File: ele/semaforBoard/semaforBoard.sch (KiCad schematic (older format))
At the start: 25 parts, among them J1 RESET, J2 Flash_connector, J3 USB_A, Q1 BC817, Q2 BC817, Q3 BC817, SW1 SW_Push, U1 ESP-01, U2 AMS1117-3.3

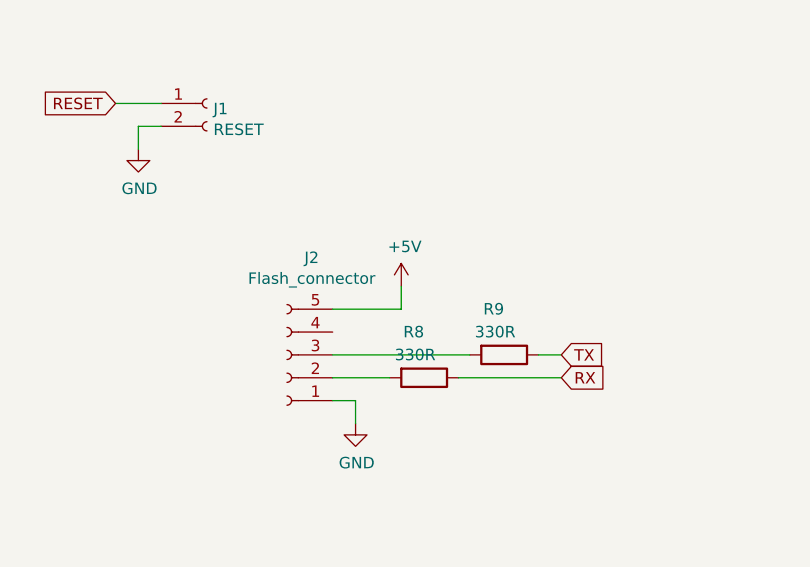
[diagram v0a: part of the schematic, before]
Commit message: Component placement, logos.
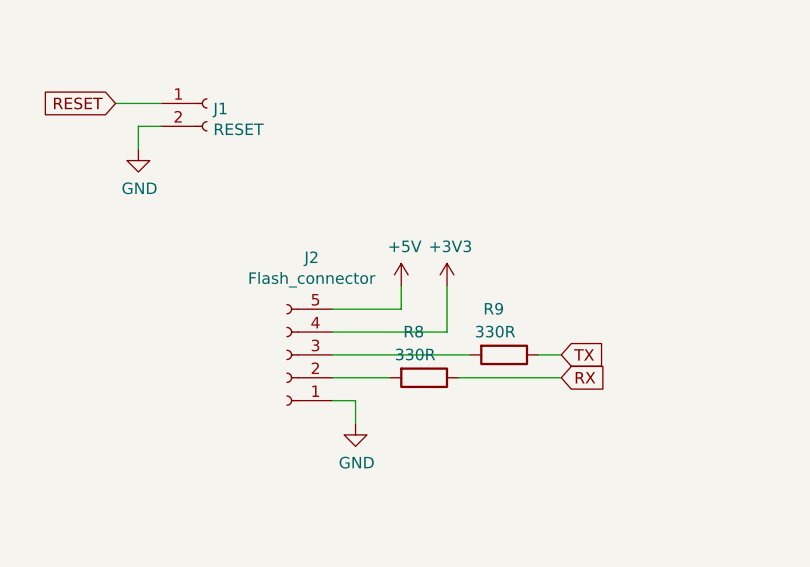
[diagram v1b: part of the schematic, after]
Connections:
- net +3V3: now also J2.4 (Pin_4)
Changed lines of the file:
@@
 	1    0    0    -1
 $EndComp
+$Comp
+L power:+3V3 #PWR?
+U 1 1 5ED38F5D
+P 6550 4250
+F 0 "#PWR?" H 6550 4100 50  0001 C CNN
+F 1 "+3V3" H 6565 4423 50  0000 C CNN
+F 2 "" H 6550 4250 50  0001 C CNN
+F 3 "" H 6550 4250 50  0001 C CNN
+	1    6550 4250
+	1    0    0    -1
+$EndComp
+Wire Wire Line
+	6550 4250 6550 4450
+Wire Wire Line
+	6550 4450 6050 4450
 $EndSCHEMATC

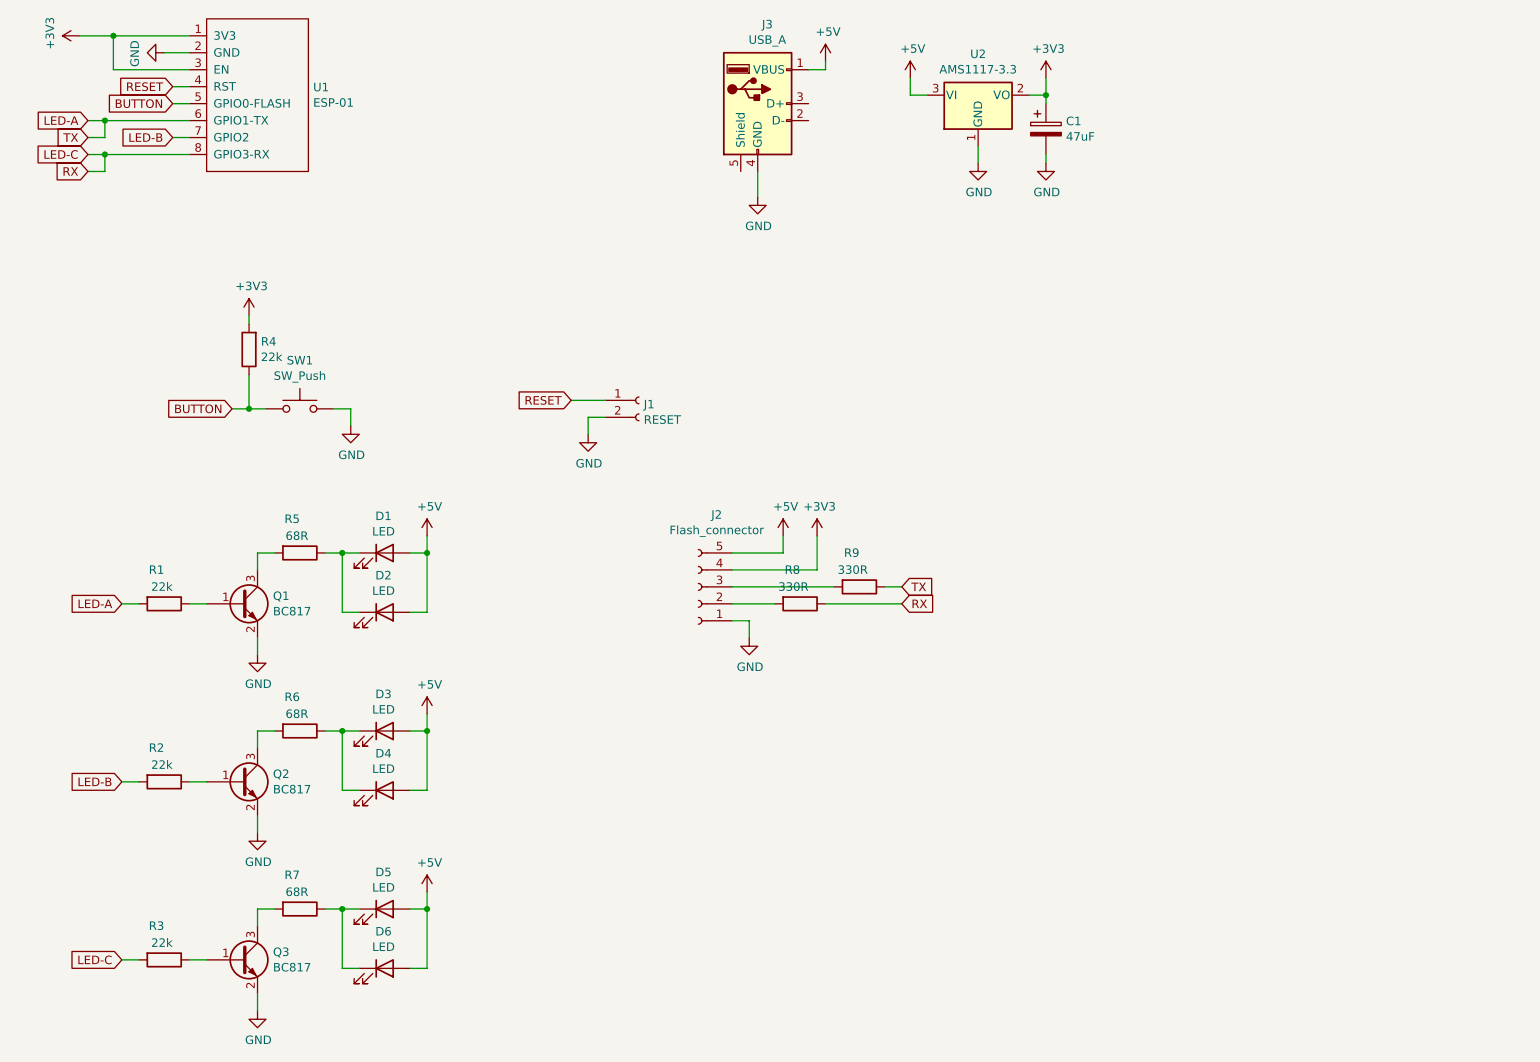
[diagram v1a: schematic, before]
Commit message: Updated schmatic for CH340G.
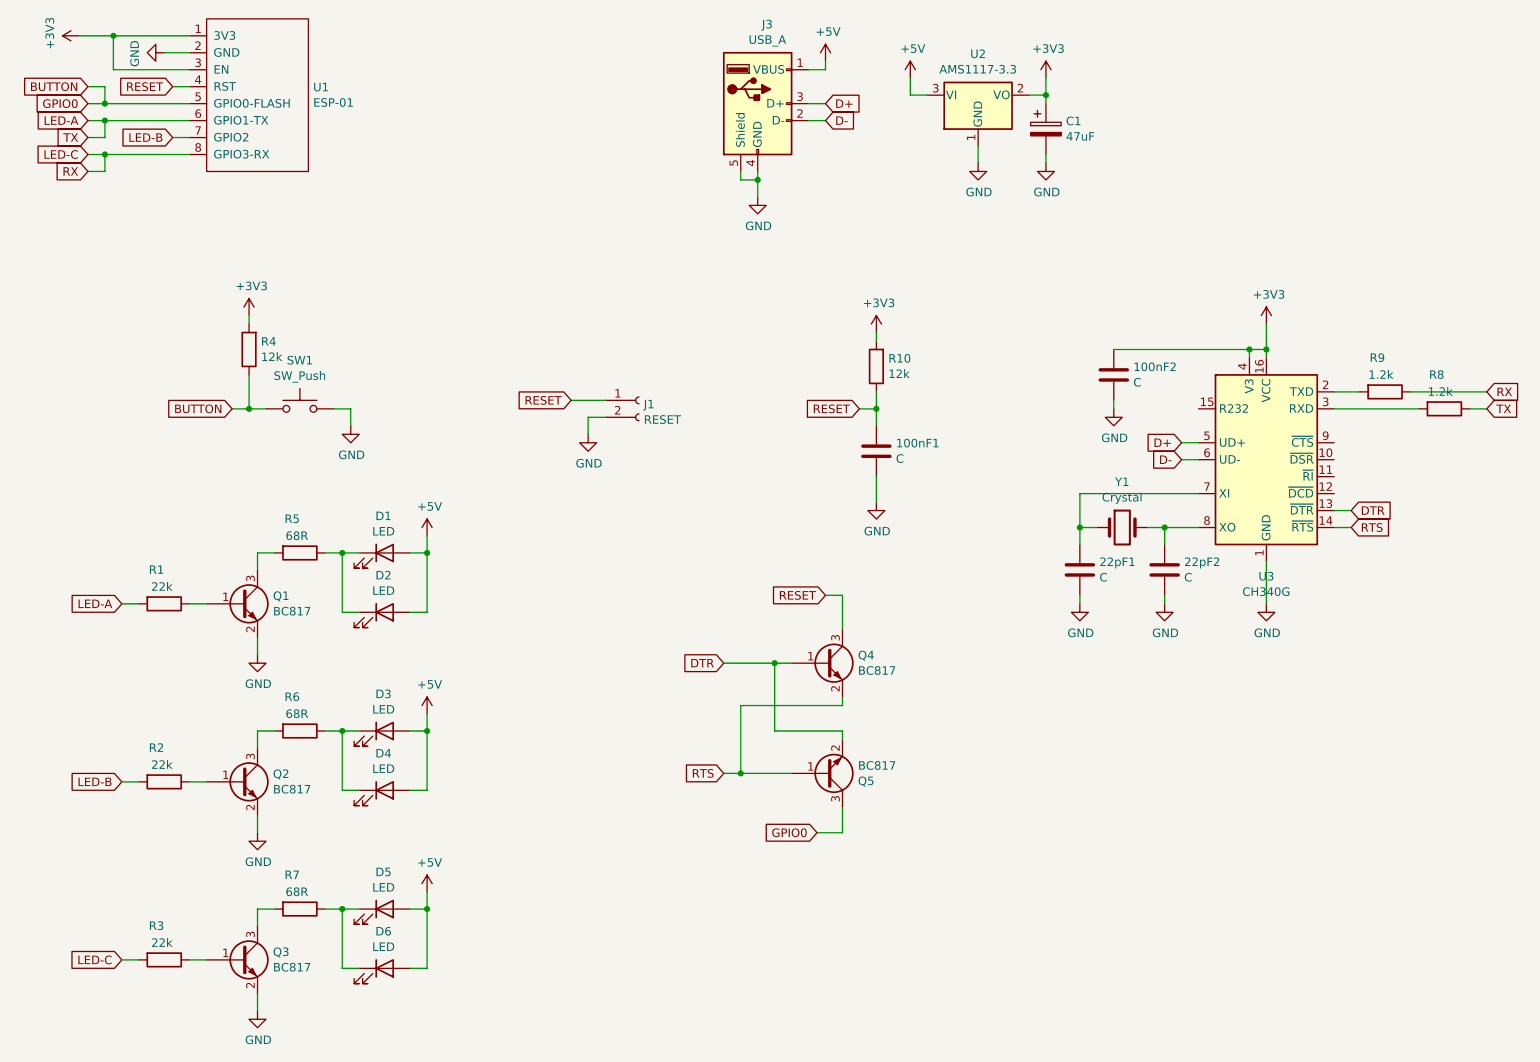
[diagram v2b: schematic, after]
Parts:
- removed J2: Flash_connector, semaforBoard:PinHeader_1x05_P2.54mm_Vertical, symbol Connector:Conn_01x05_Female
- added 100nF1, 100nF2, 22pF1, 22pF2: C, Capacitor_SMD:C_1206_3216Metric_Pad1.42x1.75mm_HandSolder, symbol Device:C
- added Q4, Q5: BC817, Package_TO_SOT_SMD:SOT-23, symbol Transistor_BJT:BC817
- added R10: 12k, Resistor_SMD:R_1206_3216Metric_Pad1.42x1.75mm_HandSolder, symbol Device:R
- added U3: CH340G, Package_SO:SOIC-16_3.9x9.9mm_P1.27mm, symbol Interface_USB:CH340G
- added Y1: Crystal, Crystal:Crystal_HC49-4H_Vertical, symbol Device:Crystal
- J1: footprint Resistor_SMD:R_1206_3216Metric_Pad1.42x1.75mm_HandSolder -> Connector_PinHeader_2.54mm:PinHeader_1x02_P2.54mm_Vertical
- R4: value 22k -> 12k
- R8, R9: value 330R -> 1.2k
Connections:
- net +3V3: now also 100nF2.1, R10.2, U3.16 (VCC), U3.4 (V3)
- net BUTTON: now also Q5.3 (C)
- net GND: now also J3.5 (Shield), 100nF1.2, 100nF2.2, 22pF1.2, 22pF2.2, U3.1 (GND)
- net LED-A: now also R8.1; no longer R9.1
- net LED-C: now also R9.1; no longer R8.1
- net RESET: now also 100nF1.1, Q4.3 (C), R10.1
- net D-: now reaches J3.2 (D-)
- net D-: now also U3.6 (UD-)
- net D+: now reaches J3.3 (D+)
- net D+: now also U3.5 (UD+)
- net at R8.2: now also U3.3 (RXD)
- net at R9.2: now also U3.2 (TXD)
- new net: 22pF1.1, U3.7 (XI), Y1.1
- new net: 22pF2.1, U3.8 (XO), Y1.2
- new net DTR: Q4.1 (B), Q5.2 (E), U3.13 (~DTR)
- new net RTS: Q4.2 (E), Q5.1 (B), U3.14 (~RTS)
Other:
- moved on the sheet: R8, R9

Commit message: 10mm leds. PCB routed.
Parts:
- C: renamed from 22pF1; value C -> 22pF
- C: renamed from 22pF2; value C -> 22pF
- C: renamed from 100nF2; value C -> 100nF
- C: renamed from 100nF1; value C -> 100nF
- D1, D2, D3, D4, D5, D6: footprint LED_THT:LED_D8.0mm -> LED_THT:LED_D10.0mm
- J1: footprint Connector_PinHeader_2.54mm:PinHeader_1x02_P2.54mm_Vertical -> semaforBoard:PinHeader_1x02_P2.54mm_Vertical
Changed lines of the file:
@@
 F 0 "D1" H 3993 4567 50  0000 C CNN
 F 1 "LED" H 3993 4476 50  0000 C CNN
-F 2 "LED_THT:LED_D8.0mm" H 4000 4350 50  0001 C CNN
+F 2 "LED_THT:LED_D10.0mm" H 4000 4350 50  0001 C CNN
 F 3 "~" H 4000 4350 50  0001 C CNN
 	1    4000 4350
@@
 F 0 "D2" H 3993 4917 50  0000 C CNN
 F 1 "LED" H 3993 4826 50  0000 C CNN
-F 2 "LED_THT:LED_D8.0mm" H 4000 4700 50  0001 C CNN
+F 2 "LED_THT:LED_D10.0mm" H 4000 4700 50  0001 C CNN
 F 3 "~" H 4000 4700 50  0001 C CNN
 	1    4000 4700
@@
 F 0 "D3" H 3993 5617 50  0000 C CNN
 F 1 "LED" H 3993 5526 50  0000 C CNN
-F 2 "LED_THT:LED_D8.0mm" H 4000 5400 50  0001 C CNN
+F 2 "LED_THT:LED_D10.0mm" H 4000 5400 50  0001 C CNN
 F 3 "~" H 4000 5400 50  0001 C CNN
 	1    4000 5400
@@
 F 0 "D4" H 3993 5967 50  0000 C CNN
 F 1 "LED" H 3993 5876 50  0000 C CNN
-F 2 "LED_THT:LED_D8.0mm" H 4000 5750 50  0001 C CNN
+F 2 "LED_THT:LED_D10.0mm" H 4000 5750 50  0001 C CNN
 F 3 "~" H 4000 5750 50  0001 C CNN
 	1    4000 5750
@@
 F 0 "D5" H 3993 6667 50  0000 C CNN
 F 1 "LED" H 3993 6576 50  0000 C CNN
-F 2 "LED_THT:LED_D8.0mm" H 4000 6450 50  0001 C CNN
+F 2 "LED_THT:LED_D10.0mm" H 4000 6450 50  0001 C CNN
 F 3 "~" H 4000 6450 50  0001 C CNN
 	1    4000 6450
@@
 F 0 "D6" H 3993 7017 50  0000 C CNN
 F 1 "LED" H 3993 6926 50  0000 C CNN
-F 2 "LED_THT:LED_D8.0mm" H 4000 6800 50  0001 C CNN
+F 2 "LED_THT:LED_D10.0mm" H 4000 6800 50  0001 C CNN
 F 3 "~" H 4000 6800 50  0001 C CNN
 	1    4000 6800
@@
 	5200 3550 5300 3550
 $Comp
-L Connector:Conn_01x02_Female J1
-U 1 1 5ECA02FE
-P 5500 3450
-F 0 "J1" H 5528 3426 50  0000 L CNN
-F 1 "RESET" H 5528 3335 50  0000 L CNN
-F 2 "Connector_PinHeader_2.54mm:PinHeader_1x02_P2.54mm_Vertical" H 5500 3450 50  0001 C CNN
-F 3 "~" H 5500 3450 50  0001 C CNN
-	1    5500 3450
-	1    0    0    -1
-$EndComp
-$Comp
 L Device:R R8
 U 1 1 5ECACA5D
@@
 $EndComp
 $Comp
-L Device:C 22pF1
+L Device:C C
 U 1 1 5EE8F2DB
 P 8100 4450
-F 0 "22pF1" H 8215 4496 50  0000 L CNN
-F 1 "C" H 8215 4405 50  0000 L CNN
+F 0 "C" H 8215 4496 50  0000 L CNN
+F 1 "22pF" H 8215 4405 50  0000 L CNN
 F 2 "Capacitor_SMD:C_1206_3216Metric_Pad1.42x1.75mm_HandSolder" H 8138 4300 50  0001 C CNN
 F 3 "~" H 8100 4450 50  0001 C CNN
@@
 $EndComp
 $Comp
-L Device:C 22pF2
+L Device:C C
 U 1 1 5EE90BE3
 P 8600 4450
-F 0 "22pF2" H 8715 4496 50  0000 L CNN
-F 1 "C" H 8715 4405 50  0000 L CNN
+F 0 "C" H 8715 4496 50  0000 L CNN
+F 1 "22pF" H 8715 4405 50  0000 L CNN
 F 2 "Capacitor_SMD:C_1206_3216Metric_Pad1.42x1.75mm_HandSolder" H 8638 4300 50  0001 C CNN
 F 3 "~" H 8600 4450 50  0001 C CNN
@@
 	9200 3150 9200 3200
 $Comp
-L Device:C 100nF2
+L Device:C C
 U 1 1 5EEBA62B
 P 8300 3300
-F 0 "100nF2" H 8415 3346 50  0000 L CNN
-F 1 "C" H 8415 3255 50  0000 L CNN
+F 0 "C" H 8415 3346 50  0000 L CNN
+F 1 "100nF" H 8415 3255 50  0000 L CNN
 F 2 "Capacitor_SMD:C_1206_3216Metric_Pad1.42x1.75mm_HandSolder" H 8338 3150 50  0001 C CNN
 F 3 "~" H 8300 3300 50  0001 C CNN
@@
 RESET
 $Comp
-L Device:C 100nF1
-U 1 1 5EEE7618
-P 6900 3750
-F 0 "100nF1" H 7015 3796 50  0000 L CNN
-F 1 "C" H 7015 3705 50  0000 L CNN
-F 2 "Capacitor_SMD:C_1206_3216Metric_Pad1.42x1.75mm_HandSolder" H 6938 3600 50  0001 C CNN
-F 3 "~" H 6900 3750 50  0001 C CNN
-	1    6900 3750
-	1    0    0    -1
-$EndComp
-$Comp
 L power:GND #PWR0124
 U 1 1 5EEEFA1C
@@
 Wire Wire Line
 	6900 3500 6900 3600
+$Comp
+L Device:C C
+U 1 1 5EEE7618
+P 6900 3750
+F 0 "C" H 7015 3796 50  0000 L CNN
+F 1 "100nF" H 7015 3705 50  0000 L CNN
+F 2 "Capacitor_SMD:C_1206_3216Metric_Pad1.42x1.75mm_HandSolder" H 6938 3600 50  0001 C CNN
+F 3 "~" H 6900 3750 50  0001 C CNN
+	1    6900 3750
+	1    0    0    -1
+$EndComp
+$Comp
+L Connector:Conn_01x02_Female J1
+U 1 1 5ECA02FE
+P 5500 3450
+F 0 "J1" H 5528 3426 50  0000 L CNN
+F 1 "RESET" H 5528 3335 50  0000 L CNN
+F 2 "semaforBoard:PinHeader_1x02_P2.54mm_Vertical" H 5500 3450 50  0001 C CNN
+F 3 "~" H 5500 3450 50  0001 C CNN
+	1    5500 3450
+	1    0    0    -1
+$EndComp
 $EndSCHEMATC

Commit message: Panelized using kikit and generated fabrication data.
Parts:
- R1, R2, R3: value 22k -> 10k
- R10, R4: value 12k -> 10k
- R5, R6, R7: value 68R -> 75R
- R8, R9: value 1.2k -> 1k
- renumbered C to C2, C to C3, C to C4, C to C5
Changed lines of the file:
@@
 P 3200 3150
 F 0 "R4" H 3130 3104 50  0000 R CNN
-F 1 "12k" H 3130 3195 50  0000 R CNN
+F 1 "10k" H 3130 3195 50  0000 R CNN
 F 2 "Resistor_SMD:R_1206_3216Metric_Pad1.42x1.75mm_HandSolder" V 3130 3150 50  0001 C CNN
 F 3 "~" H 3200 3150 50  0001 C CNN
@@
 P 3500 4350
 F 0 "R5" V 3300 4350 50  0000 R CNN
-F 1 "68R" V 3400 4400 50  0000 R CNN
+F 1 "75R" V 3400 4400 50  0000 R CNN
 F 2 "Resistor_SMD:R_1206_3216Metric_Pad1.42x1.75mm_HandSolder" V 3430 4350 50  0001 C CNN
 F 3 "~" H 3500 4350 50  0001 C CNN
@@
 P 2700 4650
 F 0 "R1" V 2500 4650 50  0000 R CNN
-F 1 "22k" V 2600 4700 50  0000 R CNN
+F 1 "10k" V 2600 4700 50  0000 R CNN
 F 2 "Resistor_SMD:R_1206_3216Metric_Pad1.42x1.75mm_HandSolder" V 2630 4650 50  0001 C CNN
 F 3 "~" H 2700 4650 50  0001 C CNN
@@
 P 3500 5400
 F 0 "R6" V 3300 5400 50  0000 R CNN
-F 1 "68R" V 3400 5450 50  0000 R CNN
+F 1 "75R" V 3400 5450 50  0000 R CNN
 F 2 "Resistor_SMD:R_1206_3216Metric_Pad1.42x1.75mm_HandSolder" V 3430 5400 50  0001 C CNN
 F 3 "~" H 3500 5400 50  0001 C CNN
@@
 P 2700 5700
 F 0 "R2" V 2500 5700 50  0000 R CNN
-F 1 "22k" V 2600 5750 50  0000 R CNN
+F 1 "10k" V 2600 5750 50  0000 R CNN
 F 2 "Resistor_SMD:R_1206_3216Metric_Pad1.42x1.75mm_HandSolder" V 2630 5700 50  0001 C CNN
 F 3 "~" H 2700 5700 50  0001 C CNN
@@
 P 3500 6450
 F 0 "R7" V 3300 6450 50  0000 R CNN
-F 1 "68R" V 3400 6500 50  0000 R CNN
+F 1 "75R" V 3400 6500 50  0000 R CNN
 F 2 "Resistor_SMD:R_1206_3216Metric_Pad1.42x1.75mm_HandSolder" V 3430 6450 50  0001 C CNN
 F 3 "~" H 3500 6450 50  0001 C CNN
@@
 P 2700 6750
 F 0 "R3" V 2500 6750 50  0000 R CNN
-F 1 "22k" V 2600 6800 50  0000 R CNN
+F 1 "10k" V 2600 6800 50  0000 R CNN
 F 2 "Resistor_SMD:R_1206_3216Metric_Pad1.42x1.75mm_HandSolder" V 2630 6750 50  0001 C CNN
 F 3 "~" H 2700 6750 50  0001 C CNN
@@
 P 10250 3500
 F 0 "R8" V 10050 3500 50  0000 R CNN
-F 1 "1.2k" V 10150 3550 50  0000 R CNN
+F 1 "1k" V 10150 3550 50  0000 R CNN
 F 2 "Resistor_SMD:R_1206_3216Metric_Pad1.42x1.75mm_HandSolder" V 10180 3500 50  0001 C CNN
 F 3 "~" H 10250 3500 50  0001 C CNN
@@
 P 9900 3400
 F 0 "R9" V 9700 3400 50  0000 R CNN
-F 1 "1.2k" V 9800 3450 50  0000 R CNN
+F 1 "1k" V 9800 3450 50  0000 R CNN
 F 2 "Resistor_SMD:R_1206_3216Metric_Pad1.42x1.75mm_HandSolder" V 9830 3400 50  0001 C CNN
 F 3 "~" H 9900 3400 50  0001 C CNN
@@
 $EndComp
 $Comp
-L Device:C C
+L Device:C C3
 U 1 1 5EE8F2DB
 P 8100 4450
-F 0 "C" H 8215 4496 50  0000 L CNN
+F 0 "C3" H 8215 4496 50  0000 L CNN
 F 1 "22pF" H 8215 4405 50  0000 L CNN
 F 2 "Capacitor_SMD:C_1206_3216Metric_Pad1.42x1.75mm_HandSolder" H 8138 4300 50  0001 C CNN
@@
 $EndComp
 $Comp
-L Device:C C
+L Device:C C5
 U 1 1 5EE90BE3
 P 8600 4450
-F 0 "C" H 8715 4496 50  0000 L CNN
+F 0 "C5" H 8715 4496 50  0000 L CNN
 F 1 "22pF" H 8715 4405 50  0000 L CNN
 F 2 "Capacitor_SMD:C_1206_3216Metric_Pad1.42x1.75mm_HandSolder" H 8638 4300 50  0001 C CNN
@@
 	9200 3150 9200 3200
 $Comp
-L Device:C C
+L Device:C C4
 U 1 1 5EEBA62B
 P 8300 3300
-F 0 "C" H 8415 3346 50  0000 L CNN
+F 0 "C4" H 8415 3346 50  0000 L CNN
 F 1 "100nF" H 8415 3255 50  0000 L CNN
 F 2 "Capacitor_SMD:C_1206_3216Metric_Pad1.42x1.75mm_HandSolder" H 8338 3150 50  0001 C CNN
@@
 P 6900 3250
 F 0 "R10" H 6830 3204 50  0000 R CNN
-F 1 "12k" H 6830 3295 50  0000 R CNN
+F 1 "10k" H 6830 3295 50  0000 R CNN
 F 2 "Resistor_SMD:R_1206_3216Metric_Pad1.42x1.75mm_HandSolder" V 6830 3250 50  0001 C CNN
 F 3 "~" H 6900 3250 50  0001 C CNN
@@
 	6900 3500 6900 3600
 $Comp
-L Device:C C
+L Device:C C2
 U 1 1 5EEE7618
 P 6900 3750
-F 0 "C" H 7015 3796 50  0000 L CNN
+F 0 "C2" H 7015 3796 50  0000 L CNN
 F 1 "100nF" H 7015 3705 50  0000 L CNN
 F 2 "Capacitor_SMD:C_1206_3216Metric_Pad1.42x1.75mm_HandSolder" H 6938 3600 50  0001 C CNN

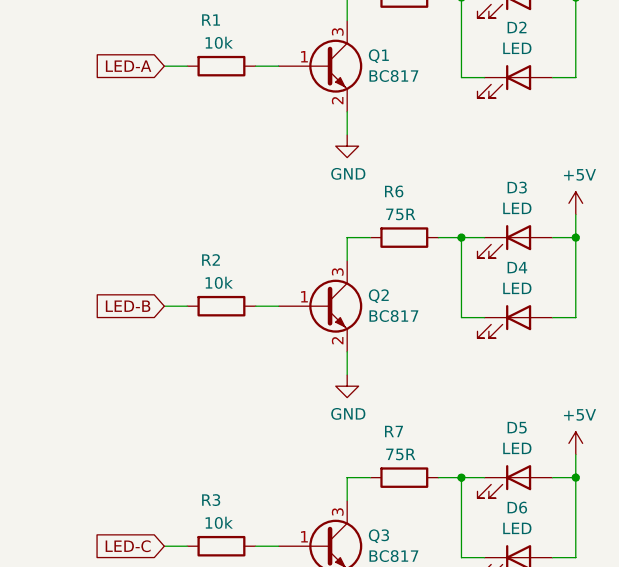
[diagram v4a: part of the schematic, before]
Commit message: Changed R2 LED-B-GPIO2 resistor from 10k to 33k for correct boot in KiCad project and excel production files. Added semafor riddle mode.
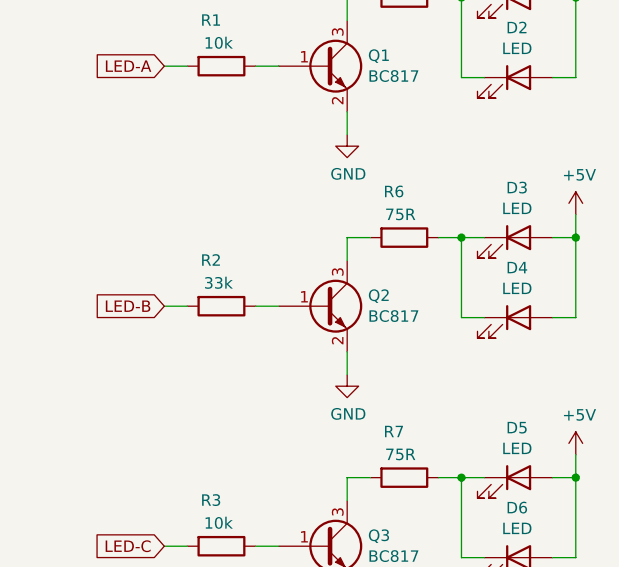
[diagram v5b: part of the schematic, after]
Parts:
- R2: value 10k -> 33k
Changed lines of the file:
@@
 P 2700 5700
 F 0 "R2" V 2500 5700 50  0000 R CNN
-F 1 "10k" V 2600 5750 50  0000 R CNN
+F 1 "33k" V 2600 5750 50  0000 R CNN
 F 2 "Resistor_SMD:R_1206_3216Metric_Pad1.42x1.75mm_HandSolder" V 2630 5700 50  0001 C CNN
 F 3 "~" H 2700 5700 50  0001 C CNN
